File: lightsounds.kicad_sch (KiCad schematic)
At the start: 27 parts, among them J1 Conn_01x03_Male, J2 Conn_01x03_Female, T1 AO3400A, T2 AO3400A, T5 AO3400A, T6 AO3400A

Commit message: unpopulate headers that are not needed
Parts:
- Boot1, EN1: now not fitted; now left out of the parts list
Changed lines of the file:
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@@
 		(unit 1)
 		(exclude_from_sim no)
-		(in_bom yes)
-		(on_board yes)
-		(dnp no)
+		(in_bom no)
+		(on_board yes)
+		(dnp yes)
 		(property "Reference" "Boot1"
 			(at 138.43 134.62 0)
@@
 		(unit 1)
 		(exclude_from_sim no)
-		(in_bom yes)
-		(on_board yes)
-		(dnp no)
+		(in_bom no)
+		(on_board yes)
+		(dnp yes)
 		(property "Reference" "EN1"
 			(at 171.45 134.62 0)

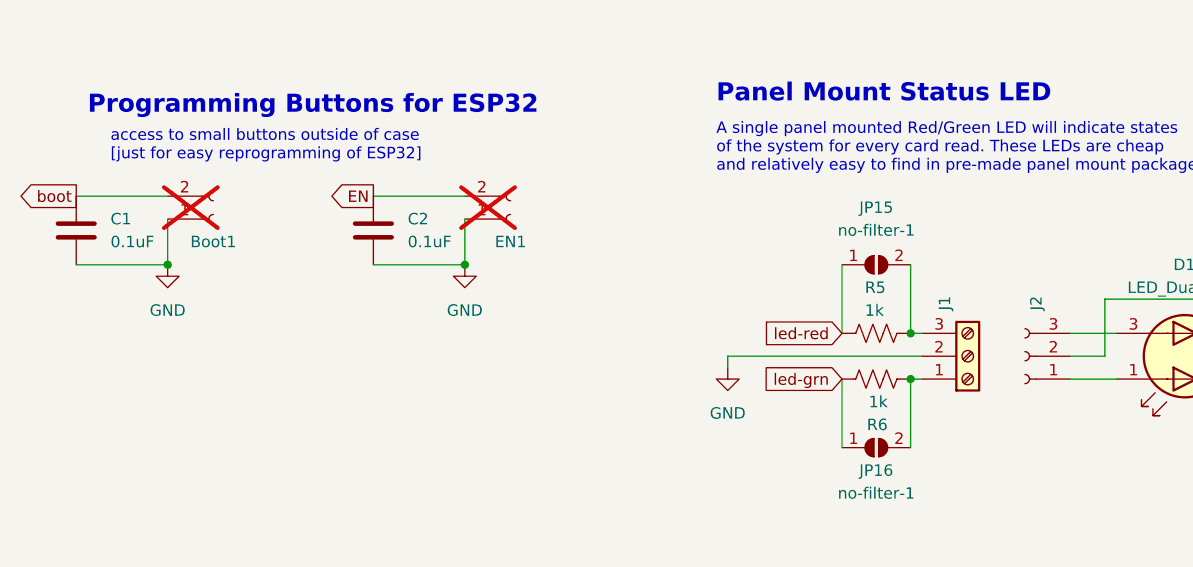
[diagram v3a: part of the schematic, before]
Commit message: convert to new parts on the board: footprint change for relay and wishlist-JST connectors
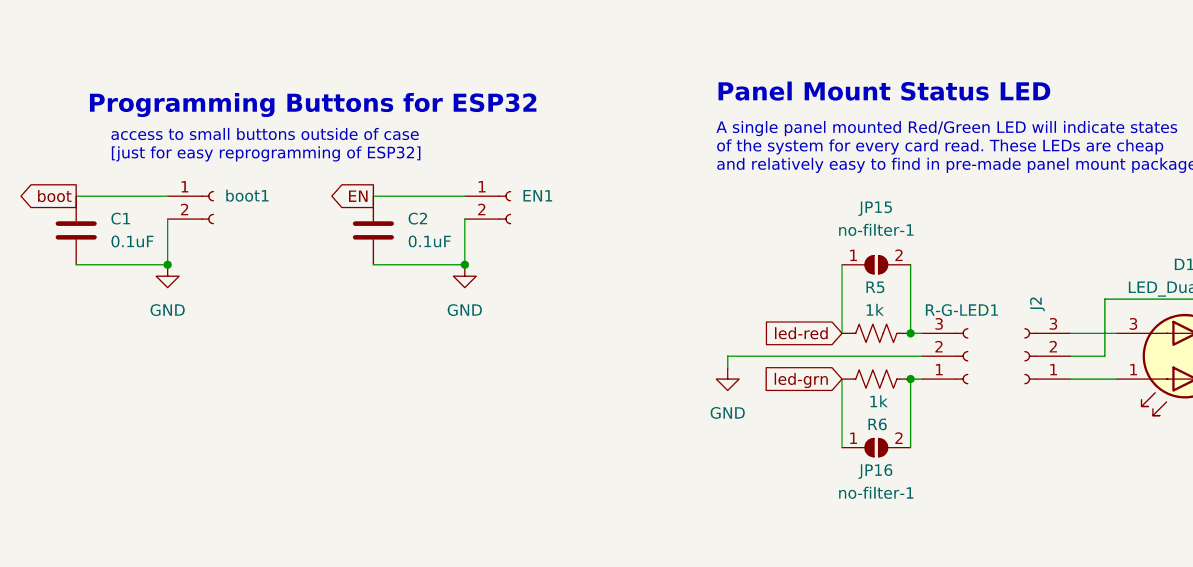
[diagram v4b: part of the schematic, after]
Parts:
- removed Boot1: Conn_01x02_Female, Connector_PinSocket_2.54mm:PinSocket_1x02_P2.54mm_Vertical, symbol Connector:Conn_01x02_Female
- removed J1: Conn_01x03_Male, TerminalBlock_TE-Connectivity:TerminalBlock_TE_282834-3_1x03_P2.54mm_Horizontal, symbol Connector:Screw_Terminal_01x03
- added R-G-LED1: Conn_01x03_Female, Connector_JST:JST_PH_B3B-PH-K_1x03_P2.00mm_Vertical, symbol Connector:Conn_01x03_Female
- added boot1: Conn_01x02_Female, Connector_JST:JST_PH_S2B-PH-K_1x02_P2.00mm_Horizontal, symbol Connector:Conn_01x02_Female
- EN1: footprint Connector_PinSocket_2.54mm:PinSocket_1x02_P2.54mm_Vertical -> Connector_JST:JST_PH_S2B-PH-K_1x02_P2.00mm_Horizontal; JLCPCB Part # (none) -> C131337; now fitted; now in the parts list
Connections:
- net EN: now also EN1.1 (Pin_1); no longer EN1.2 (Pin_2)
- net GND: now also EN1.2 (Pin_2), R-G-LED1.2 (Pin_2), boot1.2 (Pin_2); no longer EN1.1 (Pin_1)
- net boot: now also boot1.1 (Pin_1)
- net at JP16.2 (B), R6.1: now also R-G-LED1.1 (Pin_1)
- net at JP15.2 (B), R5.2: now also R-G-LED1.3 (Pin_3)
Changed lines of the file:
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@@
+	)
+	(symbol
+		(lib_id "Connector:Conn_01x02_Female")
+		(at 171.45 129.54 0)
+		(unit 1)
+		(exclude_from_sim no)
+		(in_bom yes)
+		(on_board yes)
+		(dnp no)
+		(property "Reference" "EN1"
+			(at 172.72 129.5399 0)
+			(effects
+				(font
+					(size 1.27 1.27)
+				)
+				(justify left)
+			)
+		)
+		(property "Value" "Conn_01x02_Female"
+			(at 172.72 132.0799 0)
+			(effects
+				(font
+					(size 1.27 1.27)
+				)
+				(justify left)
+				(hide yes)
+			)
+		)
+		(property "Footprint" "Connector_JST:JST_PH_S2B-PH-K_1x02_P2.00mm_Horizontal"
+			(at 171.45 129.54 0)
+			(effects
+				(font
+					(size 1.27 1.27)
+				)
+				(hide yes)
+			)
+		)
+		(property "Datasheet" "~"
+			(at 171.45 129.54 0)
+			(effects
+				(font
+					(size 1.27 1.27)
+				)
+				(hide yes)
+			)
+		)
+		(property "Description" ""
+			(at 171.45 129.54 0)
+			(effects
+				(font
+					(size 1.27 1.27)
+				)
+				(hide yes)
+			)
+		)
+		(property "JLCPCB Part #" "C131337"
+			(at 171.45 129.54 0)
+			(effects
+				(font
+					(size 1.27 1.27)
+				)
+				(hide yes)
+			)
+		)
+		(pin "1"
+		)
+		(pin "2"
+		)
+		(instances
+			(project "wing-combo"
+				(path "/586efc0f-7de2-49a7-ac21-ecfef2f716d6/3f0e9b91-fe15-47d5-84d6-aa71b368b91e/cdc711b4-3986-4d05-ace8-22e18ebb4f7d"
+					(reference "EN1")
+					(unit 1)
+				)
+			)
+		)
 	)
 	(symbol
@@
 	)
 	(symbol
+		(lib_id "Connector:Conn_01x03_Female")
+		(at 222.25 147.32 0)
+		(mirror x)
+		(unit 1)
+		(exclude_from_sim no)
+		(in_bom yes)
+		(on_board yes)
+		(dnp no)
+		(property "Reference" "R-G-LED1"
+			(at 217.424 142.24 0)
+			(effects
+				(font
+					(size 1.27 1.27)
+				)
+				(justify left)
+			)
+		)
+		(property "Value" "Conn_01x03_Female"
+			(at 224.79 148.59 0)
+			(effects
+				(font
+					(size 1.27 1.27)
+				)
+				(justify left)
+				(hide yes)
+			)
+		)
+		(property "Footprint" "Connector_JST:JST_PH_B3B-PH-K_1x03_P2.00mm_Vertical"
+			(at 222.25 147.32 0)
+			(effects
+				(font
+					(size 1.27 1.27)
+				)
+				(hide yes)
+			)
+		)
+		(property "Datasheet" "~"
+			(at 222.25 147.32 0)
+			(effects
+				(font
+					(size 1.27 1.27)
+				)
+				(hide yes)
+			)
+		)
+		(property "Description" ""
+			(at 222.25 147.32 0)
+			(effects
+				(font
+					(size 1.27 1.27)
+				)
+				(hide yes)
+			)
+		)
+		(property "JLCPCB Part #" "C131339"
+			(at 222.25 147.32 0)
+			(effects
+				(font
+					(size 1.27 1.27)
+				)
+				(hide yes)
+			)
+		)
+		(pin "1"
+		)
+		(pin "2"
+		)
+		(pin "3"
+		)
+		(instances
+			(project "wing-combo"
+				(path "/586efc0f-7de2-49a7-ac21-ecfef2f716d6/3f0e9b91-fe15-47d5-84d6-aa71b368b91e/cdc711b4-3986-4d05-ace8-22e18ebb4f7d"
+					(reference "R-G-LED1")
+					(unit 1)
+				)
+			)
+		)
+	)
+	(symbol
 		(lib_id "Device:R_US")
 		(at 212.09 144.78 90)
@@
 	)
 	(symbol
-		(lib_id "Connector:Conn_01x02_Female")
-		(at 138.43 132.08 0)
-		(mirror x)
-		(unit 1)
-		(exclude_from_sim no)
-		(in_bom no)
-		(on_board yes)
-		(dnp yes)
-		(property "Reference" "Boot1"
-			(at 138.43 134.62 0)
-			(effects
-				(font
-					(size 1.27 1.27)
-				)
-			)
-		)
-		(property "Value" "Conn_01x02_Female"
-			(at 139.7 129.5401 0)
-			(effects
-				(font
-					(size 1.27 1.27)
-				)
-				(justify left)
-				(hide yes)
-			)
-		)
-		(property "Footprint" "Connector_PinSocket_2.54mm:PinSocket_1x02_P2.54mm_Vertical"
-			(at 138.43 132.08 0)
-			(effects
-				(font
-					(size 1.27 1.27)
-				)
-				(hide yes)
-			)
-		)
-		(property "Datasheet" "~"
-			(at 138.43 132.08 0)
-			(effects
-				(font
-					(size 1.27 1.27)
-				)
-				(hide yes)
-			)
-		)
-		(property "Description" ""
-			(at 138.43 132.08 0)
-			(effects
-				(font
-					(size 1.27 1.27)
-				)
-				(hide yes)
-			)
-		)
-		(pin "1"
-		)
-		(pin "2"
-		)
-		(instances
-			(project "wing-combo"
-				(path "/586efc0f-7de2-49a7-ac21-ecfef2f716d6/3f0e9b91-fe15-47d5-84d6-aa71b368b91e/cdc711b4-3986-4d05-ace8-22e18ebb4f7d"
-					(reference "Boot1")
-					(unit 1)
-				)
-			)
-		)
-	)
-	(symbol
 		(lib_id "Device:C")
 		(at 156.21 133.35 0)
@@
 	)
 	(symbol
-		(lib_id "Connector:Screw_Terminal_01x03")
-		(at 222.25 147.32 0)
-		(mirror x)
-		(unit 1)
-		(exclude_from_sim no)
-		(in_bom yes)
-		(on_board yes)
-		(dnp no)
-		(property "Reference" "J1"
-			(at 219.71 142.24 90)
-			(effects
-				(font
-					(size 1.27 1.27)
-				)
-				(justify right)
-			)
-		)
-		(property "Value" "Conn_01x03_Male"
-			(at 223.52 135.89 0)
-			(effects
-				(font
-					(size 1.27 1.27)
-				)
-				(justify right)
-				(hide yes)
-			)
-		)
-		(property "Footprint" "TerminalBlock_TE-Connectivity:TerminalBlock_TE_282834-3_1x03_P2.54mm_Horizontal"
-			(at 222.25 147.32 0)
-			(effects
-				(font
-					(size 1.27 1.27)
-				)
-				(hide yes)
-			)
-		)
-		(property "Datasheet" "~"
-			(at 222.25 147.32 0)
-			(effects
-				(font
-					(size 1.27 1.27)
-				)
-				(hide yes)
-			)
-		)
-		(property "Description" ""
-			(at 222.25 147.32 0)
-			(effects
-				(font
-					(size 1.27 1.27)
-				)
-				(hide yes)
-			)
-		)
-		(property "JLCPCB Part #" "C557686"
-			(at 222.25 147.32 90)
-			(effects
-				(font
-					(size 1.27 1.27)
-				)
-				(hide yes)
-			)
-		)
-		(pin "1"
-		)
-		(pin "2"
-		)
-		(pin "3"
-		)
-		(instances
-			(project "wing-combo"
-				(path "/586efc0f-7de2-49a7-ac21-ecfef2f716d6/3f0e9b91-fe15-47d5-84d6-aa71b368b91e/cdc711b4-3986-4d05-ace8-22e18ebb4f7d"
-					(reference "J1")
-					(unit 1)
-				)
-			)
-		)
-	)
-	(symbol
 		(lib_id "Device:R_US")
 		(at 44.45 171.45 180)
@@
 	(symbol
 		(lib_id "Connector:Conn_01x02_Female")
-		(at 171.45 132.08 0)
-		(mirror x)
-		(unit 1)
-		(exclude_from_sim no)
-		(in_bom no)
-		(on_board yes)
-		(dnp yes)
-		(property "Reference" "EN1"
-			(at 171.45 134.62 0)
-			(effects
-				(font
-					(size 1.27 1.27)
-				)
+		(at 138.43 129.54 0)
+		(unit 1)
+		(exclude_from_sim no)
+		(in_bom yes)
+		(on_board yes)
+		(dnp no)
+		(property "Reference" "boot1"
+			(at 139.7 129.5399 0)
+			(effects
+				(font
+					(size 1.27 1.27)
+				)
+				(justify left)
 			)
 		)
 		(property "Value" "Conn_01x02_Female"
-			(at 172.72 129.5401 0)
-			(effects
-				(font
-					(size 1.27 1.27)
-				)
-				(justify left)
-				(hide yes)
-			)
-		)
-		(property "Footprint" "Connector_PinSocket_2.54mm:PinSocket_1x02_P2.54mm_Vertical"
-			(at 171.45 132.08 0)
+			(at 139.7 132.0799 0)
+			(effects
+				(font
+					(size 1.27 1.27)
+				)
+				(justify left)
+				(hide yes)
+			)
+		)
+		(property "Footprint" "Connector_JST:JST_PH_S2B-PH-K_1x02_P2.00mm_Horizontal"
+			(at 138.43 129.54 0)
 			(effects
 				(font
@@
 		)
 		(property "Datasheet" "~"
-			(at 171.45 132.08 0)
-			(effects
-				(font
-					(size 1.27 1.27)
-				)
-				(hide yes)
-			)
-		)
-		(property "Description" ""
-			(at 171.45 132.08 0)
-			(effects
-				(font
-					(size 1.27 1.27)
-				)
-				(hide yes)
-			)
-		)
-		(pin "1"
-		)
-		(pin "2"
-		)
-		(instances
-			(project "wing-combo"
-				(path "/586efc0f-7de2-49a7-ac21-ecfef2f716d6/3f0e9b91-fe15-47d5-84d6-aa71b368b91e/cdc711b4-3986-4d05-ace8-22e18ebb4f7d"
-					(reference "EN1")
-					(unit 1)
-				)
+			(at 138.43 129.54 0)
+			(effects
+				(font
+					(size 1.27 1.27)
+				)
+				(hide yes)
+			)
+		)
+		(property "Description" ""
+			(at 138.43 129.54 0)
+			(effects
+				(font
+					(size 1.27 1.27)
+				)
+				(hide yes)
+			)
+		)
+		(property "JLCPCB Part #" "C131337"
+			(at 138.43 129.54 0)
+			(effects
+				(font
+					(size 1.27 1.27)
+				)
+				(hide yes)
+			)
+		)
+		(pin "1"
+		)
+		(pin "2"
+		)
+		(instances
+			(project "wing-combo"
+				(path "/586efc0f-7de2-49a7-ac21-ecfef2f716d6/3f0e9b91-fe15-47d5-84d6-aa71b368b91e/cdc711b4-3986-4d05-ace8-22e18ebb4f7d"
+					(reference "boot1")
+					(unit 1)
+				)

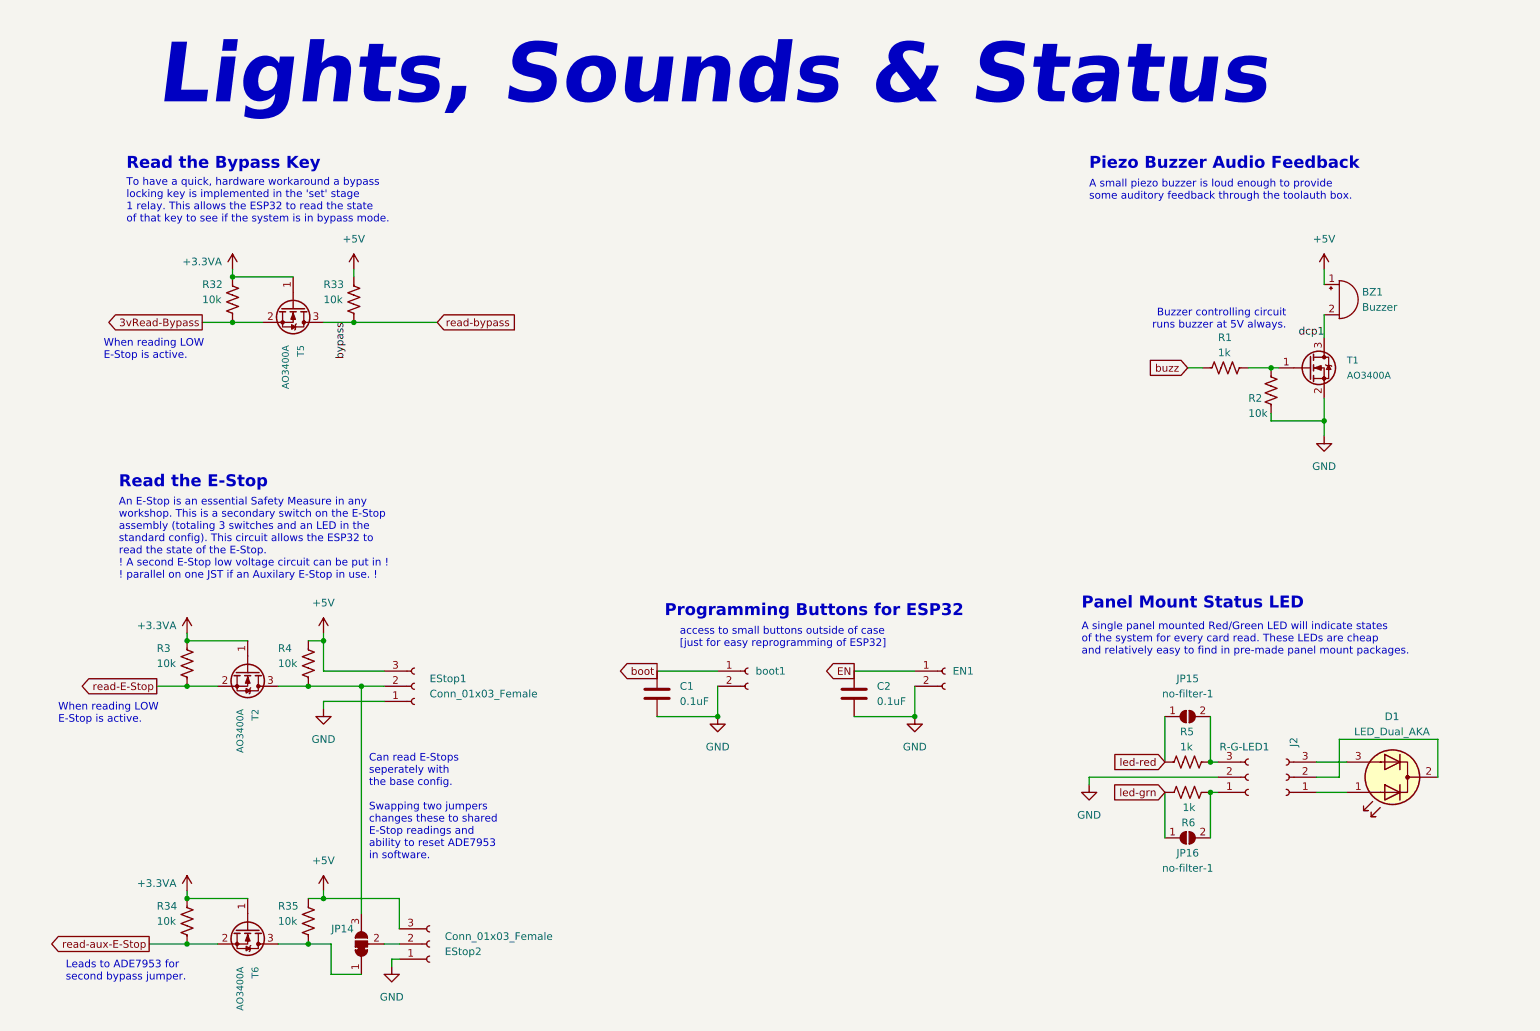
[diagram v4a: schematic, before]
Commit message: reassigned netclasses, removed vestigial level-shifter
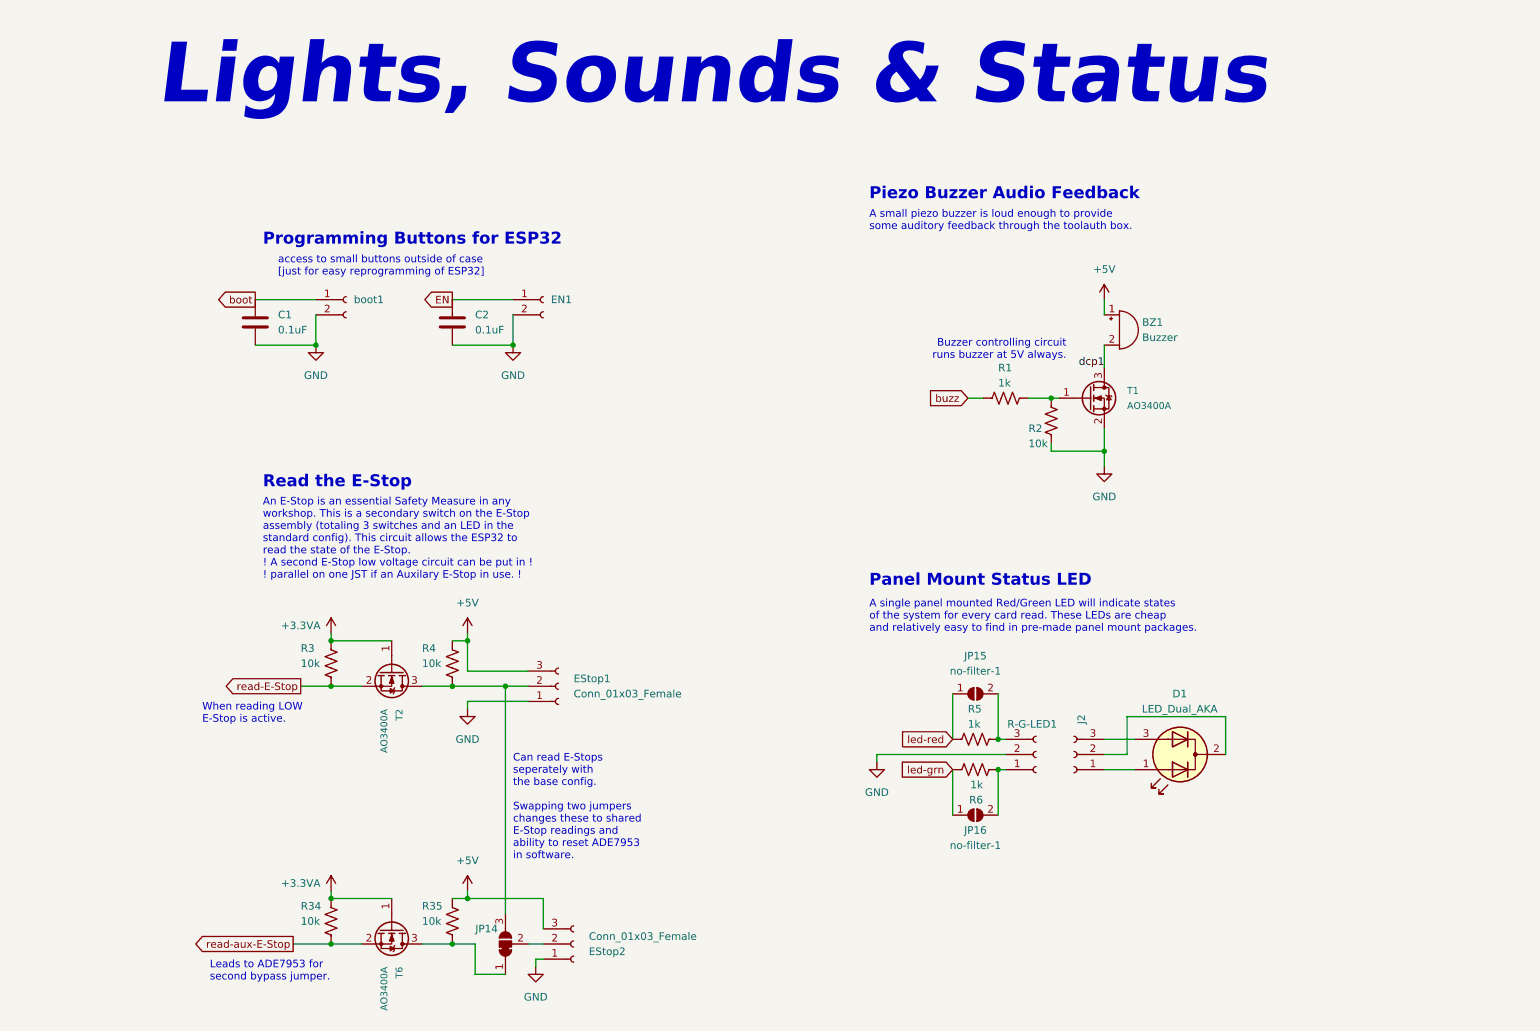
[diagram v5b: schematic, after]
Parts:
- removed R32, R33: 10k, Resistor_SMD:R_0603_1608Metric, symbol Device:R_US
- removed T5: AO3400A, Package_TO_SOT_SMD:SOT-23, symbol Transistor_FET:AO3400A
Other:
- note removed: "Read the Bypass Key"
- note removed: "To have a quick, hardware workaround a bypass locking key is implemented in the 'set' stage 1 relay. This allows the ESP32 to read the state of that key to see if the system is in bypass mode."
- moved on the sheet: BZ1, C1, C2, D1, EN1, EStop1, EStop2, J2, JP14, JP15, JP16, R-G-LED1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

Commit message: added 3D models to design
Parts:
- BZ1: footprint Buzzer_Beeper:Buzzer_12x9.5RM7.6 -> buzzer:BUZ-TH_BD12.0-P7.60-D0.6-FD
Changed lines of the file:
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@@
 			)
 		)
-		(property "Footprint" "Buzzer_Beeper:Buzzer_12x9.5RM7.6"
+		(property "Footprint" "buzzer:BUZ-TH_BD12.0-P7.60-D0.6-FD"
 			(at 200.025 69.85 90)
 			(effects
